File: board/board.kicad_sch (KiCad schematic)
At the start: 3 parts, among them Q1 NPN

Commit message: Added some components
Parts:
- added C1, C2, C3: C, symbol Device:C
- added J1: Screw_Terminal_01x02, symbol Connector:Screw_Terminal_01x02
- added Q2: NPN, symbol Simulation_SPICE:NPN
- added R3, R4, R5, R6, R7, R8: R, symbol Device:R
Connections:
- net 9V: now reaches R2.1
- net 9V: now also R7.1
- net at Q1.2 (B), R1.1: now also C1.2, C2.1, R4.1
- net at Q1.3 (E): now also R3.1, R5.2
- new net: Q2.3 (E), R8.1
- new net: C1.1, J1.2 (Pin_2)
- new net: C3.1, R5.1
- new net: C3.2, Q2.2 (B), R6.1
- new net: Q2.1 (C), R7.2
- new net GND: C2.2, J1.1 (Pin_1), R3.2, R4.2, R8.2
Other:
- moved on the sheet: Q1, R1, R2

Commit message: Complete schematic
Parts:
- added C4, C5, C6, C7, C8, C9: C, symbol Device:C
- added D1: D_Zener, symbol Device:D_Zener
- added J2: Screw_Terminal_01x02, symbol Connector:Screw_Terminal_01x02
- added L1: L, symbol Device:L
- added Q3: NPN, symbol Simulation_SPICE:NPN
- added R10, R11, R12, R13, R14, R9: R, symbol Device:R
- added RV1: R_Potentiometer, symbol Device:R_Potentiometer
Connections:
- net 9V: now also C8.1, C9.1, D1.1 (K), R13.1
- net GND: now also C5.2, C8.2, C9.2, D1.2 (A), J2.2 (Pin_2), R12.2, R14.2, RV1.3
- net at Q2.1 (C), R7.2: now also C4.1, R10.1, R9.1
- net at R6.2: now also C7.1, L1.2, R11.2
- new net: C6.2, Q3.2 (B), R10.2
- new net: C4.2, J2.1 (Pin_1), RV1.1
- new net: C6.1, RV1.2
- new net: C7.2, Q3.3 (E), R14.1
- new net: C5.1, L1.1, R11.1, R12.1, R9.2
- new net: Q3.1 (C), R13.2

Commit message: Updates PCB file
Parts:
- C1, C2, C3, C4, C5, C6, C7, C8, C9: footprint (none) -> Capacitor_THT:CP_Radial_D8.0mm_P5.00mm
- D1: footprint (none) -> Diode_THT:D_DO-41_SOD81_P10.16mm_Horizontal
- J1, J2: footprint (none) -> TerminalBlock_4Ucon:TerminalBlock_4Ucon_1x02_P3.50mm_Horizontal
- L1: footprint (none) -> Inductor_THT:L_Radial_D16.8mm_P12.70mm_Vishay_IHB-1
- Q2, Q3: footprint (none) -> Package_TO_SOT_THT:TO-92
- R10, R11, R12, R13, R14, R3, R4, R5, R6, R7, R8, R9: footprint (none) -> Resistor_THT:R_Axial_DIN0309_L9.0mm_D3.2mm_P15.24mm_Horizontal
- RV1: footprint (none) -> Connector_Wuerth:Wuerth_WR-WTB_64800311622_1x03_P1.50mm_Vertical
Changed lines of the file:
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@@
       (effects (font (size 1.27 1.27)) (justify left))
     )
-    (property "Footprint" "" (at 36.5252 163.83 0)
+    (property "Footprint" "Capacitor_THT:CP_Radial_D8.0mm_P5.00mm" (at 36.5252 163.83 0)
       (effects (font (size 1.27 1.27)) hide)
     )
@@
       (effects (font (size 1.27 1.27)))
     )
-    (property "Footprint" "" (at 172.72 76.708 90)
+    (property "Footprint" "Resistor_THT:R_Axial_DIN0309_L9.0mm_D3.2mm_P15.24mm_Horizontal" (at 172.72 76.708 90)
       (effects (font (size 1.27 1.27)) hide)
     )
@@
       (effects (font (size 1.27 1.27)) (justify left))
     )
-    (property "Footprint" "" (at 135.382 107.95 90)
+    (property "Footprint" "Resistor_THT:R_Axial_DIN0309_L9.0mm_D3.2mm_P15.24mm_Horizontal" (at 135.382 107.95 90)
       (effects (font (size 1.27 1.27)) hide)
     )
@@
       (effects (font (size 1.27 1.27)) (justify right))
     )
-    (property "Footprint" "" (at 203.2 95.25 0)
+    (property "Footprint" "Connector_Wuerth:Wuerth_WR-WTB_64800311622_1x03_P1.50mm_Vertical" (at 203.2 95.25 0)
       (effects (font (size 1.27 1.27)) hide)
     )
@@
       (effects (font (size 1.27 1.27)))
     )
-    (property "Footprint" "" (at 55.88 84.1248 0)
+    (property "Footprint" "Capacitor_THT:CP_Radial_D8.0mm_P5.00mm" (at 55.88 84.1248 0)
       (effects (font (size 1.27 1.27)) hide)
     )
@@
       (effects (font (size 1.27 1.27)))
     )
-    (property "Footprint" "" (at 196.85 127.3048 0)
+    (property "Footprint" "Capacitor_THT:CP_Radial_D8.0mm_P5.00mm" (at 196.85 127.3048 0)
       (effects (font (size 1.27 1.27)) hide)
     )
@@
       (effects (font (size 1.27 1.27)) (justify left))
     )
-    (property "Footprint" "" (at 183.642 107.95 90)
+    (property "Footprint" "Resistor_THT:R_Axial_DIN0309_L9.0mm_D3.2mm_P15.24mm_Horizontal" (at 183.642 107.95 90)
       (effects (font (size 1.27 1.27)) hide)
     )
@@
       (effects (font (size 1.27 1.27)) (justify left))
     )
-    (property "Footprint" "" (at 155.702 107.95 90)
+    (property "Footprint" "Resistor_THT:R_Axial_DIN0309_L9.0mm_D3.2mm_P15.24mm_Horizontal" (at 155.702 107.95 90)
       (effects (font (size 1.27 1.27)) hide)
     )
@@
       (effects (font (size 1.27 1.27)) (justify left))
     )
-    (property "Footprint" "" (at 84.582 107.95 90)
+    (property "Footprint" "Resistor_THT:R_Axial_DIN0309_L9.0mm_D3.2mm_P15.24mm_Horizontal" (at 84.582 107.95 90)
       (effects (font (size 1.27 1.27)) hide)
     )
@@
       (effects (font (size 1.27 1.27)) (justify left))
     )
-    (property "Footprint" "" (at 49.2252 163.83 0)
+    (property "Footprint" "Capacitor_THT:CP_Radial_D8.0mm_P5.00mm" (at 49.2252 163.83 0)
       (effects (font (size 1.27 1.27)) hide)
     )
@@
       (effects (font (size 1.27 1.27)))
     )
-    (property "Footprint" "" (at 31.75 87.63 0)
+    (property "Footprint" "TerminalBlock_4Ucon:TerminalBlock_4Ucon_1x02_P3.50mm_Horizontal" (at 31.75 87.63 0)
       (effects (font (size 1.27 1.27)) hide)
     )
@@
       (effects (font (size 1.27 1.27)) (justify left))
     )
-    (property "Footprint" "" (at 56.642 107.95 90)
+    (property "Footprint" "Resistor_THT:R_Axial_DIN0309_L9.0mm_D3.2mm_P15.24mm_Horizontal" (at 56.642 107.95 90)
       (effects (font (size 1.27 1.27)) hide)
     )
@@
       (effects (font (size 1.27 1.27)) (justify left))
     )
-    (property "Footprint" "" (at 72.0852 111.76 0)
+    (property "Footprint" "Capacitor_THT:CP_Radial_D8.0mm_P5.00mm" (at 72.0852 111.76 0)
       (effects (font (size 1.27 1.27)) hide)
     )
@@
       (effects (font (size 1.27 1.27)))
     )
-    (property "Footprint" "" (at 119.38 91.7448 0)
+    (property "Footprint" "Capacitor_THT:CP_Radial_D8.0mm_P5.00mm" (at 119.38 91.7448 0)
       (effects (font (size 1.27 1.27)) hide)
     )
@@
       (effects (font (size 1.27 1.27)) (justify left))
     )
-    (property "Footprint" "" (at 171.1452 111.76 0)
+    (property "Footprint" "Capacitor_THT:CP_Radial_D8.0mm_P5.00mm" (at 171.1452 111.76 0)
       (effects (font (size 1.27 1.27)) hide)
     )
@@
       (effects (font (size 1.27 1.27)) (justify left))
     )
-    (property "Footprint" "" (at 135.382 80.01 90)
+    (property "Footprint" "Resistor_THT:R_Axial_DIN0309_L9.0mm_D3.2mm_P15.24mm_Horizontal" (at 135.382 80.01 90)
       (effects (font (size 1.27 1.27)) hide)
     )
@@
       (effects (font (size 1.27 1.27)) (justify left))
     )
-    (property "Footprint" "" (at 297.18 95.25 0)
+    (property "Footprint" "Package_TO_SOT_THT:TO-92" (at 297.18 95.25 0)
       (effects (font (size 1.27 1.27)) hide)
     )
@@
       (effects (font (size 1.27 1.27)))
     )
-    (property "Footprint" "" (at 102.87 90.932 90)
+    (property "Footprint" "Resistor_THT:R_Axial_DIN0309_L9.0mm_D3.2mm_P15.24mm_Horizontal" (at 102.87 90.932 90)
       (effects (font (size 1.27 1.27)) hide)
     )
@@
       (effects (font (size 1.27 1.27)) (justify left))
     )
-    (property "Footprint" "" (at 234.442 110.49 90)
+    (property "Footprint" "Resistor_THT:R_Axial_DIN0309_L9.0mm_D3.2mm_P15.24mm_Horizontal" (at 234.442 110.49 90)
       (effects (font (size 1.27 1.27)) hide)
     )
@@
       (effects (font (size 1.27 1.27)) (justify left))
     )
-    (property "Footprint" "" (at 234.442 78.74 90)
+    (property "Footprint" "Resistor_THT:R_Axial_DIN0309_L9.0mm_D3.2mm_P15.24mm_Horizontal" (at 234.442 78.74 90)
       (effects (font (size 1.27 1.27)) hide)
     )
@@
       (effects (font (size 1.27 1.27)) (justify left))
     )
-    (property "Footprint" "" (at 148.59 107.95 0)
+    (property "Footprint" "Inductor_THT:L_Radial_D16.8mm_P12.70mm_Vishay_IHB-1" (at 148.59 107.95 0)
       (effects (font (size 1.27 1.27)) hide)
     )
@@
       (effects (font (size 1.27 1.27)) (justify left))
     )
-    (property "Footprint" "" (at 257.81 93.98 0)
+    (property "Footprint" "TerminalBlock_4Ucon:TerminalBlock_4Ucon_1x02_P3.50mm_Horizontal" (at 257.81 93.98 0)
       (effects (font (size 1.27 1.27)) hide)
     )
@@
       (effects (font (size 1.27 1.27)) (justify left))
     )
-    (property "Footprint" "" (at 198.12 92.71 0)
+    (property "Footprint" "Package_TO_SOT_THT:TO-92" (at 198.12 92.71 0)
       (effects (font (size 1.27 1.27)) hide)
     )
@@
       (effects (font (size 1.27 1.27)))
     )
-    (property "Footprint" "" (at 222.25 94.2848 0)
+    (property "Footprint" "Capacitor_THT:CP_Radial_D8.0mm_P5.00mm" (at 222.25 94.2848 0)
       (effects (font (size 1.27 1.27)) hide)
     )
@@
       (effects (font (size 1.27 1.27)) (justify left))
     )
-    (property "Footprint" "" (at 121.412 100.33 90)
+    (property "Footprint" "Resistor_THT:R_Axial_DIN0309_L9.0mm_D3.2mm_P15.24mm_Horizontal" (at 121.412 100.33 90)
       (effects (font (size 1.27 1.27)) hide)
     )
@@
       (effects (font (size 1.27 1.27)) (justify left))
     )
-    (property "Footprint" "" (at 60.96 160.02 0)
+    (property "Footprint" "Diode_THT:D_DO-41_SOD81_P10.16mm_Horizontal" (at 60.96 160.02 0)
       (effects (font (size 1.27 1.27)) hide)
     )
@@
       (effects (font (size 1.27 1.27)) (justify left))
     )
-    (property "Footprint" "" (at 155.702 93.98 90)
+    (property "Footprint" "Resistor_THT:R_Axial_DIN0309_L9.0mm_D3.2mm_P15.24mm_Horizontal" (at 155.702 93.98 90)
       (effects (font (size 1.27 1.27)) hide)
     )
@@
       (effects (font (size 1.27 1.27)))
     )
-    (property "Footprint" "" (at 176.53 84.1248 0)
-      (effects (font (size 1.27 1.27)) hide)
-    )
+    (property "Footprint" "Capacitor_THT:CP_Radial_D8.0mm_P5.00mm" (at 176.53 84.1248 0)
+      (effects (font (size 1.27 1.27)) hide)
+    )

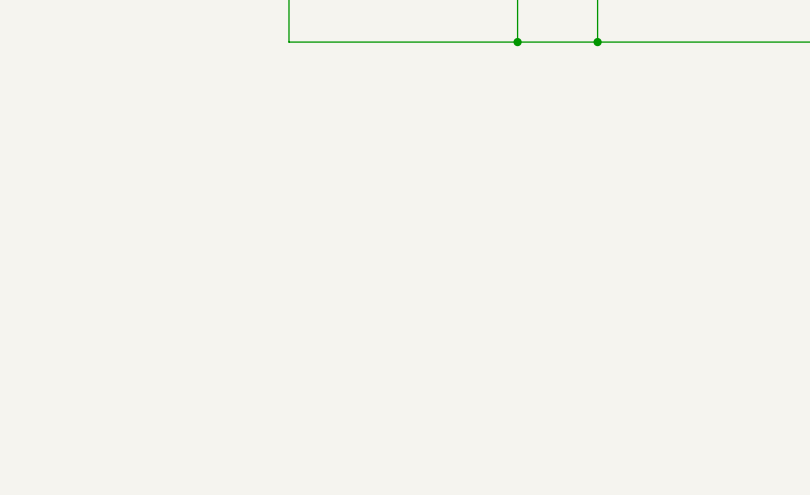
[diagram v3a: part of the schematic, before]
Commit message: Updates PCB file
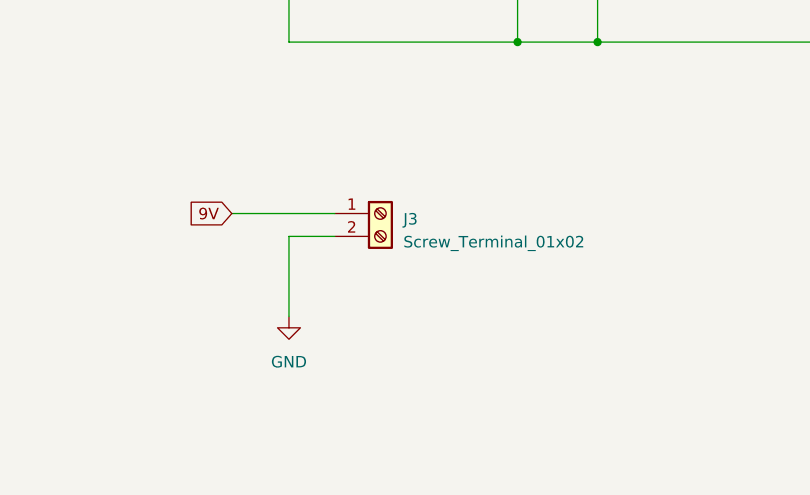
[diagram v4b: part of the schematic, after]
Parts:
- added J3: Screw_Terminal_01x02, TerminalBlock_4Ucon:TerminalBlock_4Ucon_1x02_P3.50mm_Horizontal, symbol Connector:Screw_Terminal_01x02
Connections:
- net 9V: now also J3.1 (Pin_1)
- net GND: now also J3.2 (Pin_2)
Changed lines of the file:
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@@
+    (stroke (width 0) (type default))
+  )
+  (wire (pts (xy 123.19 149.86) (xy 123.19 158.75))
     (stroke (width 0) (type default))
   )
@@
     (stroke (width 0) (type default))
   )
+  (wire (pts (xy 128.27 149.86) (xy 123.19 149.86))
+    (stroke (width 0) (type default))
+  )
   (wire (pts (xy 148.59 128.27) (xy 157.48 128.27))
     (stroke (width 0) (type default))
@@
   )
   (wire (pts (xy 168.91 74.93) (xy 157.48 74.93))
+    (stroke (width 0) (type default))
+  )
+  (wire (pts (xy 116.84 147.32) (xy 128.27 147.32))
     (stroke (width 0) (type default))
   )
@@
     )
   )
+  (global_label "9V" (shape input) (at 116.84 147.32 180) (fields_autoplaced)
+    (effects (font (size 1.27 1.27)) (justify right))
+    (property "Intersheetrefs" "${INTERSHEET_REFS}" (at 111.6361 147.32 0)
+      (effects (font (size 1.27 1.27)) (justify right) hide)
+    )
+  )
   (global_label "9V" (shape input) (at 133.35 66.04 180) (fields_autoplaced)
     (effects (font (size 1.27 1.27)) (justify right))
@@
     )
   )
+  (symbol (lib_id "Connector:Screw_Terminal_01x02") (at 133.35 147.32 0) (unit 1)
+    (in_bom yes) (on_board yes) (dnp no) (fields_autoplaced)
+    (property "Reference" "J3" (at 135.89 147.955 0)
+      (effects (font (size 1.27 1.27)) (justify left))
+    )
+    (property "Value" "Screw_Terminal_01x02" (at 135.89 150.495 0)
+      (effects (font (size 1.27 1.27)) (justify left))
+    )
+    (property "Footprint" "TerminalBlock_4Ucon:TerminalBlock_4Ucon_1x02_P3.50mm_Horizontal" (at 133.35 147.32 0)
+      (effects (font (size 1.27 1.27)) hide)
+    )
+    (property "Datasheet" "~" (at 133.35 147.32 0)
+      (effects (font (size 1.27 1.27)) hide)
+    )
+    (pin "1")
+    (pin "2")
+    (instances
+      (project "board"
+        (path "/955dd638-810f-48c9-87a2-b8c09d3c2ba3"
+          (reference "J3") (unit 1)
+        )
+      )
+    )
+  )
   (symbol (lib_id "Device:C") (at 35.56 160.02 0) (unit 1)
     (in_bom yes) (on_board yes) (dnp no) (fields_autoplaced)
@@
         )
       )
+    )
+  )
+  (symbol (lib_id "power:GND") (at 123.19 158.75 0) (unit 1)
+    (in_bom yes) (on_board yes) (dnp no) (fields_autoplaced)
+    (property "Reference" "#PWR012" (at 123.19 165.1 0)
+      (effects (font (size 1.27 1.27)) hide)
+    )
+    (property "Value" "GND" (at 123.19 163.83 0)
+      (effects (font (size 1.27 1.27)))
+    )
+    (property "Footprint" "" (at 123.19 158.75 0)
+      (effects (font (size 1.27 1.27)) hide)
+    )
+    (property "Datasheet" "" (at 123.19 158.75 0)
+      (effects (font (size 1.27 1.27)) hide)
+    )
+    (pin "1")
+    (instances
+      (project "board"
+        (path "/955dd638-810f-48c9-87a2-b8c09d3c2ba3"
+          (reference "#PWR012") (unit 1)
+        )
+      )
